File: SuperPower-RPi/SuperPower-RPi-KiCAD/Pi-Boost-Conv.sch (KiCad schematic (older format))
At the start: 0 parts

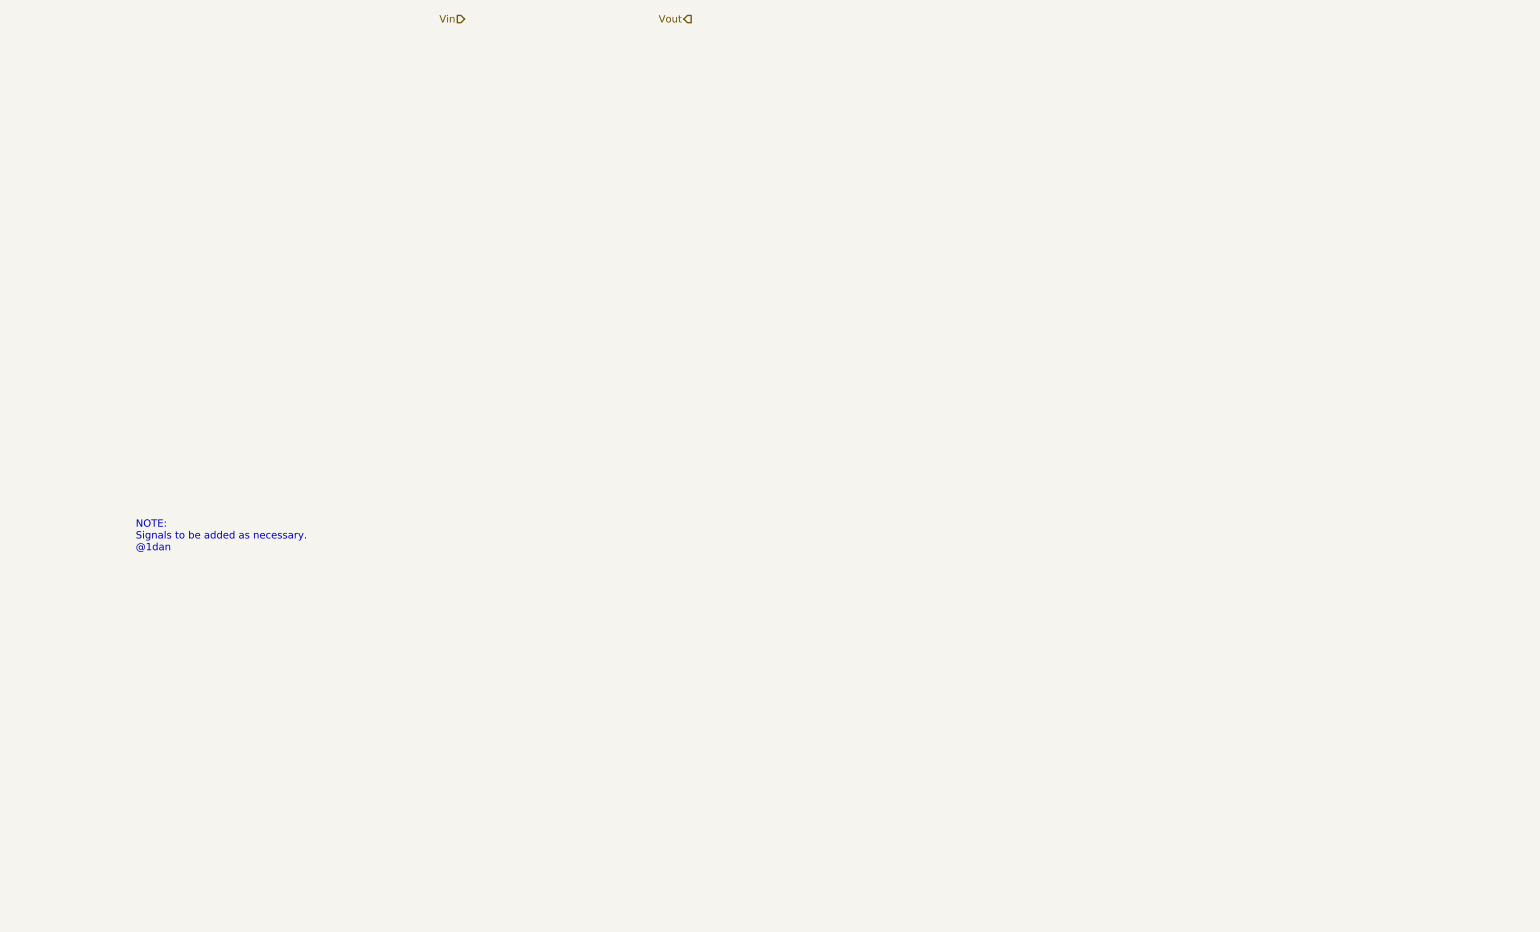
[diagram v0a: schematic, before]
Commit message: Basic component setup for the boost converter, added TPS61088 symbol to 'Manual_Lib' Library
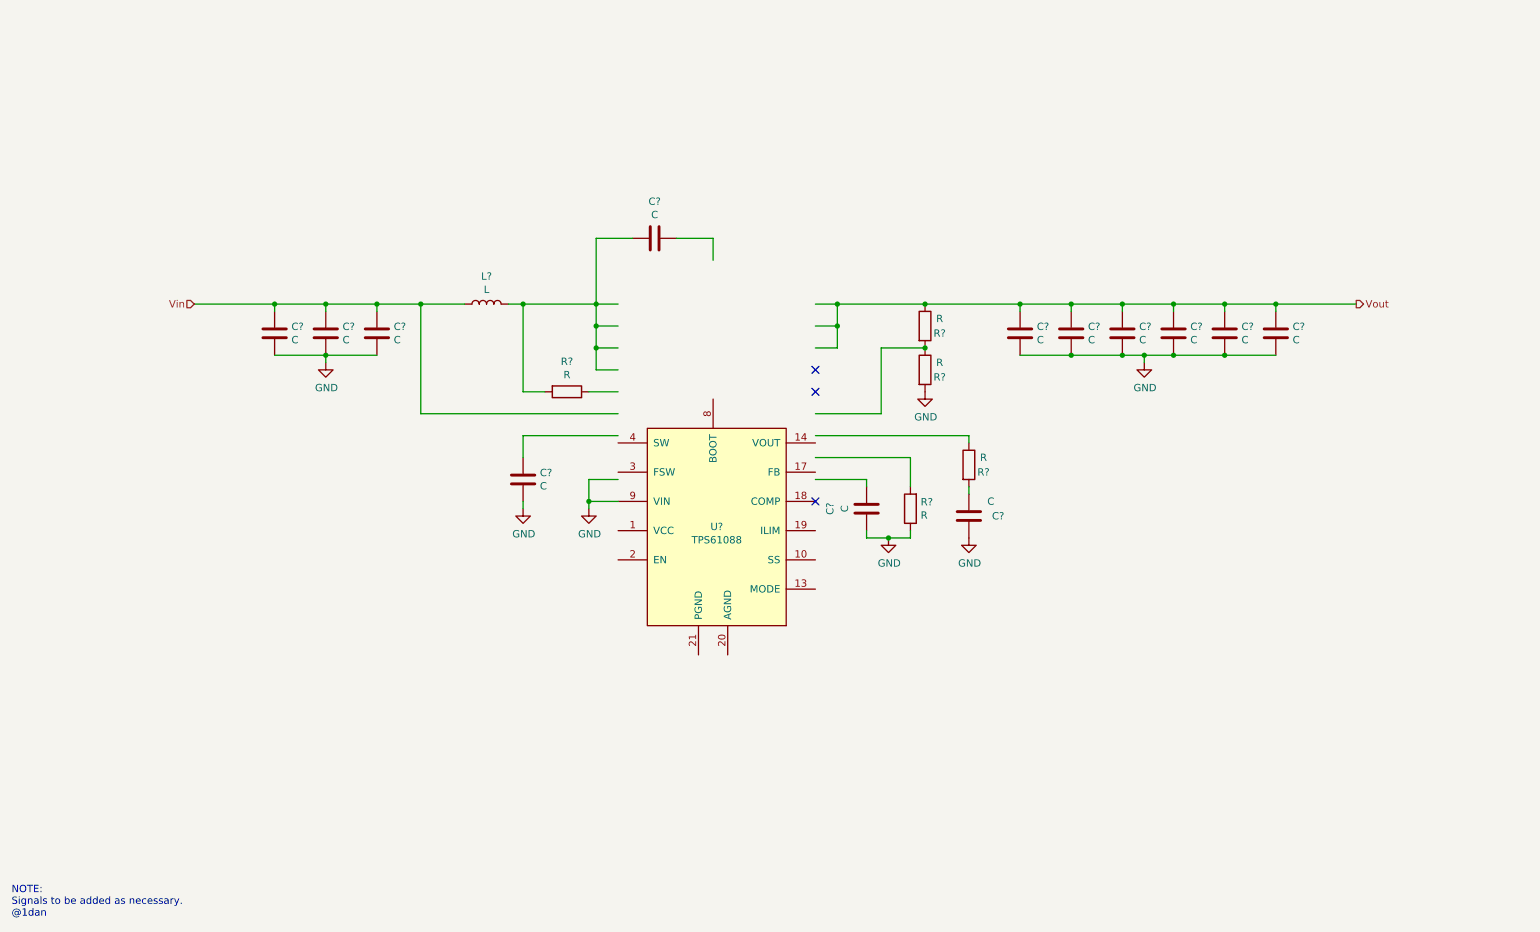
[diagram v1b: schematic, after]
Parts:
- added C? (x13): C, symbol Device:C
- added L?: L, symbol Device:L
- added R? (x5): R, symbol Device:R
- added U?: TPS61088, symbol Manual_Lib:TPS61088
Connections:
- net labels added: GND
- wire segments 0 -> 76
- no-connect marks 0 -> 3

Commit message: Basic component values added to boost ocnverter
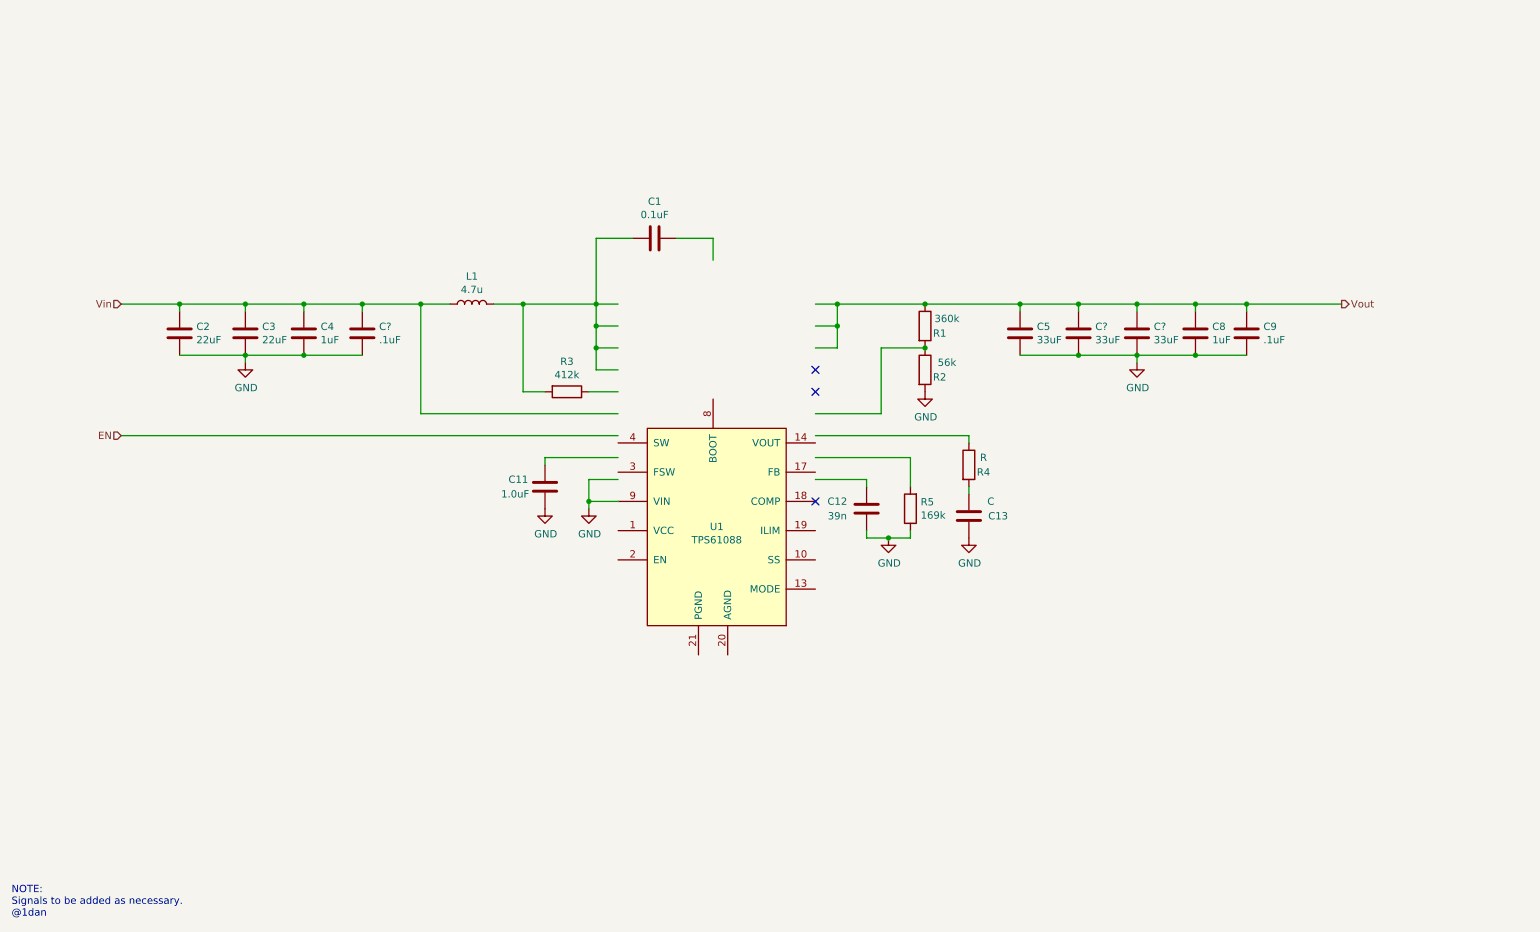
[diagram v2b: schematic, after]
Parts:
- removed C? (x3): C, symbol Device:C
- removed U?: TPS61088, symbol Manual_Lib:TPS61088
- added C? (x2): 33uF, symbol Device:C
- added C?: .1uF, symbol Device:C
- added U1: TPS61088, symbol Manual_Lib:TPS61088
- C1: renamed from C?; value C -> 0.1uF
- C11: renamed from C?; value C -> 1.0uF
- C12: renamed from C?; value C -> 39n
- C2, C3: renamed from C?; value C -> 22uF
- C4, C8: renamed from C?; value C -> 1uF
- C5: renamed from C?; value C -> 33uF
- C9: renamed from C?; value C -> .1uF
- L1: renamed from L?; value L -> 4.7u
- R1: renamed from R?; value R -> 360k
- R2: renamed from R?; value R -> 56k
- R3: renamed from R?; value R -> 412k
- R5: renamed from R?; value R -> 169k
- gave numbers to parts that had none: 2
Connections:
- net labels added: EN
- wire segments 76 -> 75
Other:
- moved on the sheet: C11, C2, C3, C4, C8, C9, L1

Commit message: Added charger circuitry, and updated boost converter.
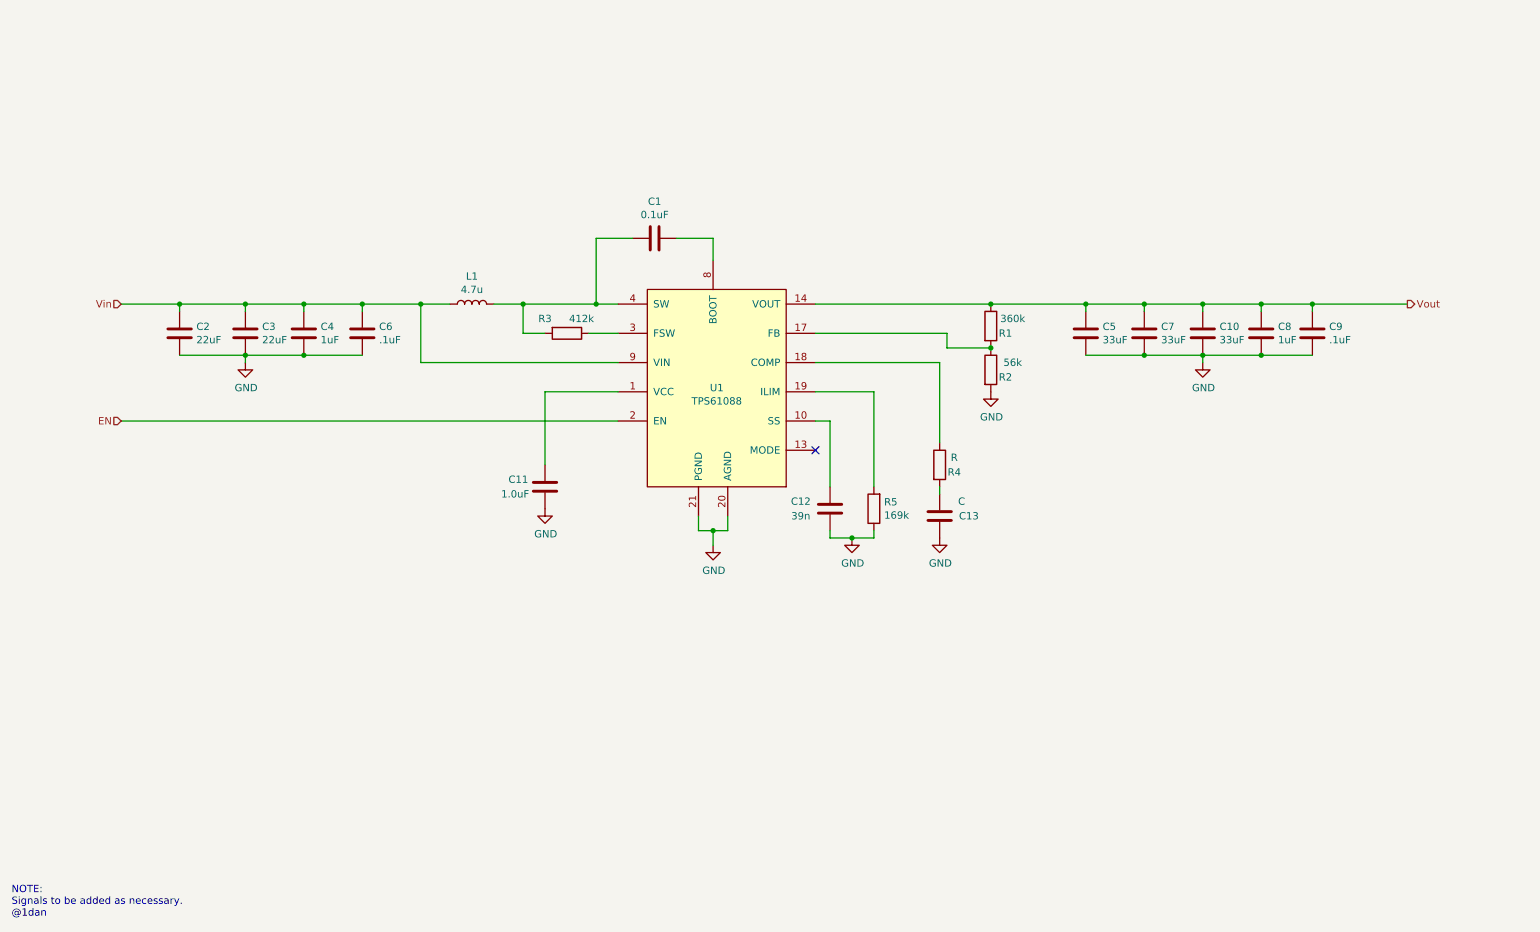
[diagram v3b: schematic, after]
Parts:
- gave numbers to parts that had none: 3
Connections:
- wire segments 75 -> 65
- no-connect marks 3 -> 1
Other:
- moved on the sheet: C10, C12, C13, C5, C7, C8, C9, R1, R2, R3, R4, R5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

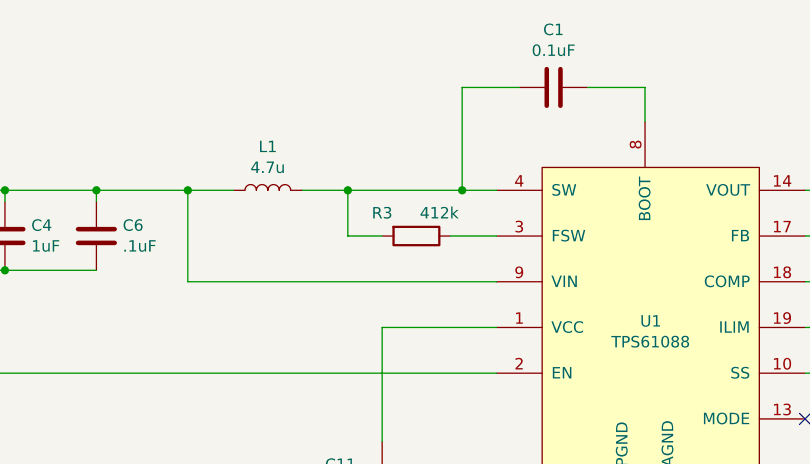
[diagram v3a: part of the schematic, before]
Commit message: Updated TPS61088 part to clear up ERC errors.
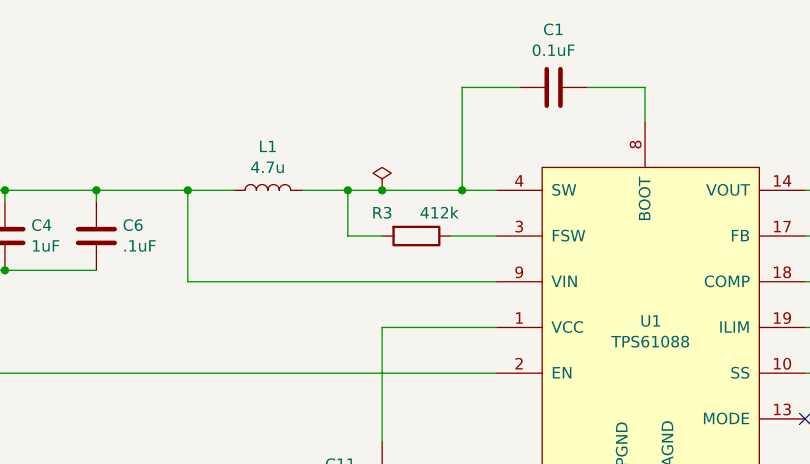
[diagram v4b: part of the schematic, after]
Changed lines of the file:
@@
 	4650 3400 4800 3400
 Wire Wire Line
-	4650 3400 4150 3400
+	4650 3400 4300 3400
 Connection ~ 4650 3400
 Wire Wire Line
@@
 Wire Wire Line
 	7000 3800 7000 4350
+$Comp
+L power:PWR_FLAG #FLG0105
+U 1 1 5F799D48
+P 4300 3400
+F 0 "#FLG0105" H 4300 3475 50  0001 C CNN
+F 1 "PWR_FLAG" H 4300 3573 50  0001 C CNN
+F 2 "" H 4300 3400 50  0001 C CNN
+F 3 "~" H 4300 3400 50  0001 C CNN
+	1    4300 3400
+	1    0    0    -1
+$EndComp
+Connection ~ 4300 3400
+Wire Wire Line
+	4300 3400 4150 3400
 $EndSCHEMATC

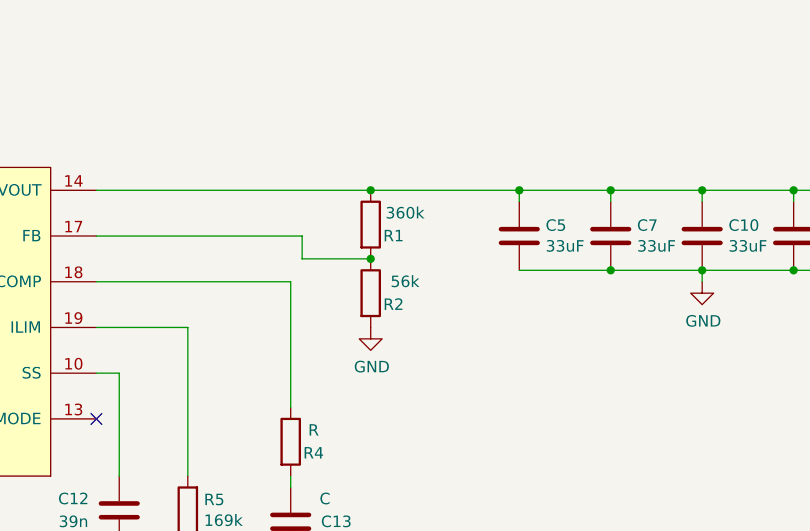
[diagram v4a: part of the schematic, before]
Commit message: Updated Boost Converter's feedback Resistor values
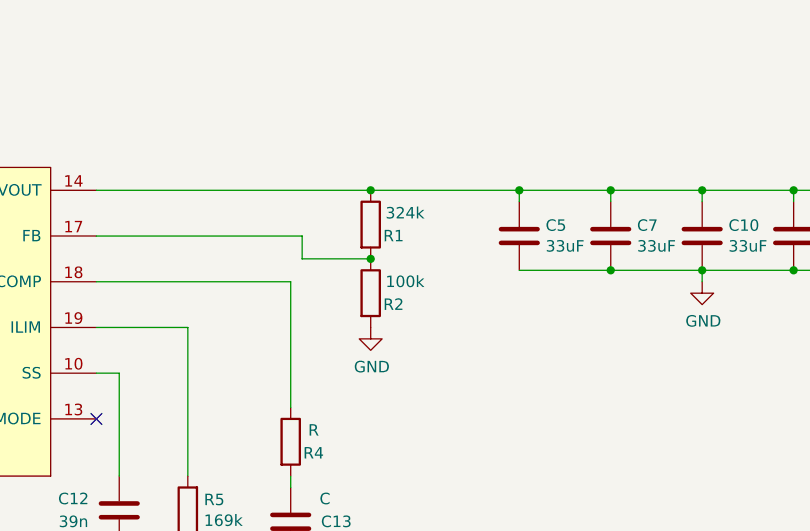
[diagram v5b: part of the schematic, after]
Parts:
- R1: value 360k -> 324k
- R2: value 56k -> 100k
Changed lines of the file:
@@
 P 7350 3850
 F 0 "R2" H 7450 3800 50  0000 C CNN
-F 1 "56k" H 7500 3900 50  0000 C CNN
+F 1 "100k" H 7500 3900 50  0000 C CNN
 F 2 "" V 7280 3850 50  0001 C CNN
 F 3 "~" H 7350 3850 50  0001 C CNN
@@
 P 7350 3550
 F 0 "R1" H 7450 3500 50  0000 C CNN
-F 1 "360k" H 7500 3600 50  0000 C CNN
+F 1 "324k" H 7500 3600 50  0000 C CNN
 F 2 "" V 7280 3550 50  0001 C CNN
 F 3 "~" H 7350 3550 50  0001 C CNN

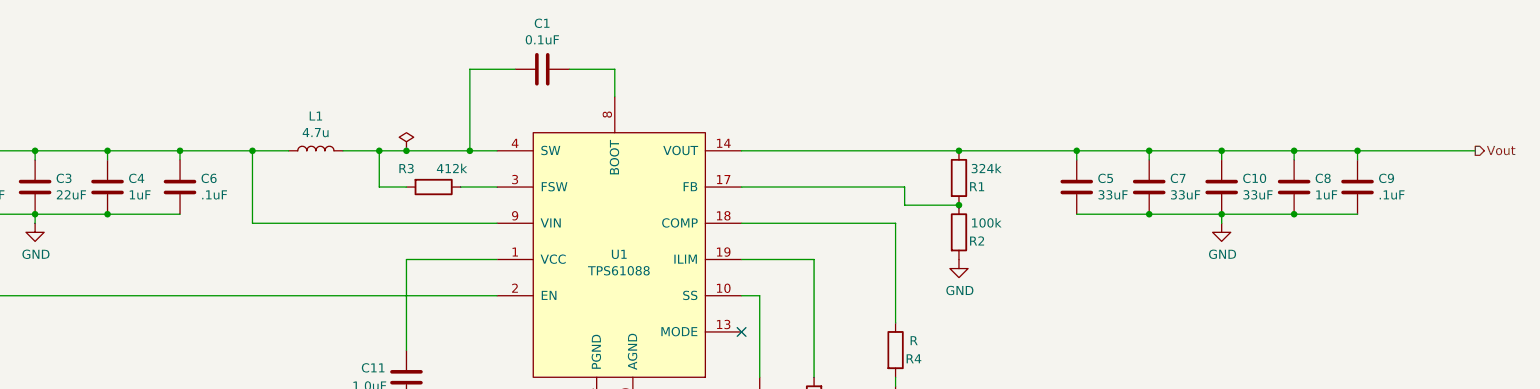
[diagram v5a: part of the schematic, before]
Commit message: Added overvoltag protection. Discussed on discord on 10/10/2020
(cherry picked from commit 123c8c775d478169a35a5854a68dc219ac457a44)
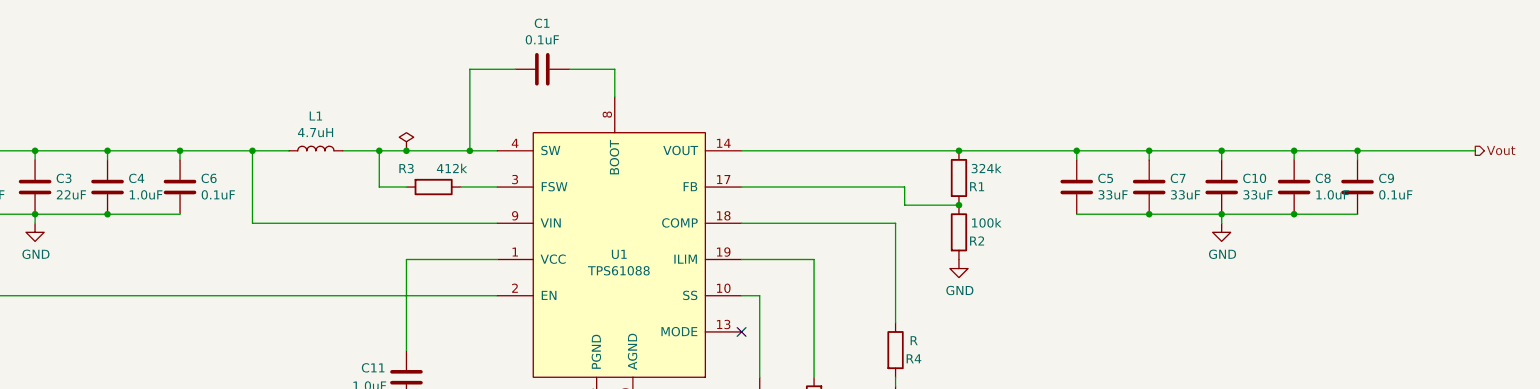
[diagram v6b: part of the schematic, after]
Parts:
- C1, C12: footprint (none) -> Capacitor_SMD:C_0603_1608Metric
- C4, C8: value 1uF -> 1.0uF
- C6, C9: value .1uF -> 0.1uF; footprint (none) -> Capacitor_SMD:C_0603_1608Metric
- L1: value 4.7u -> 4.7uH
- R1, R2, R3: footprint (none) -> Resistor_SMD:R_0603_1608Metric
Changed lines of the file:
@@
 P 3800 3400
 F 0 "L1" V 3990 3400 50  0000 C CNN
-F 1 "4.7u" V 3899 3400 50  0000 C CNN
+F 1 "4.7uH" V 3899 3400 50  0000 C CNN
 F 2 "" H 3800 3400 50  0001 C CNN
 F 3 "~" H 3800 3400 50  0001 C CNN
@@
 F 0 "R3" V 4350 3450 50  0000 C CNN
 F 1 "412k" V 4350 3700 50  0000 C CNN
-F 2 "" V 4380 3600 50  0001 C CNN
+F 2 "Resistor_SMD:R_0603_1608Metric" V 4380 3600 50  0001 C CNN
 F 3 "~" H 4450 3600 50  0001 C CNN
 	1    4450 3600
@@
 P 2650 3600
 F 0 "C4" H 2765 3646 50  0000 L CNN
-F 1 "1uF" H 2765 3555 50  0000 L CNN
+F 1 "1.0uF" H 2765 3555 50  0000 L CNN
 F 2 "" H 2688 3450 50  0001 C CNN
 F 3 "~" H 2650 3600 50  0001 C CNN
@@
 P 9200 3600
 F 0 "C8" H 9315 3646 50  0000 L CNN
-F 1 "1uF" H 9315 3555 50  0000 L CNN
+F 1 "1.0uF" H 9315 3555 50  0000 L CNN
 F 2 "" H 9238 3450 50  0001 C CNN
 F 3 "~" H 9200 3600 50  0001 C CNN
@@
 P 9550 3600
 F 0 "C9" H 9665 3646 50  0000 L CNN
-F 1 ".1uF" H 9665 3555 50  0000 L CNN
-F 2 "" H 9588 3450 50  0001 C CNN
+F 1 "0.1uF" H 9665 3555 50  0000 L CNN
+F 2 "Capacitor_SMD:C_0603_1608Metric" H 9588 3450 50  0001 C CNN
 F 3 "~" H 9550 3600 50  0001 C CNN
 	1    9550 3600
@@
 F 0 "C1" V 4798 2950 50  0000 C CNN
 F 1 "0.1uF" V 4889 2950 50  0000 C CNN
-F 2 "" H 5088 2800 50  0001 C CNN
+F 2 "Capacitor_SMD:C_0603_1608Metric" H 5088 2800 50  0001 C CNN
 F 3 "~" H 5050 2950 50  0001 C CNN
 	1    5050 2950
@@
 F 0 "R2" H 7450 3800 50  0000 C CNN
 F 1 "100k" H 7500 3900 50  0000 C CNN
-F 2 "" V 7280 3850 50  0001 C CNN
+F 2 "Resistor_SMD:R_0603_1608Metric" V 7280 3850 50  0001 C CNN
 F 3 "~" H 7350 3850 50  0001 C CNN
 	1    7350 3850
@@
 F 0 "R1" H 7450 3500 50  0000 C CNN
 F 1 "324k" H 7500 3600 50  0000 C CNN
-F 2 "" V 7280 3550 50  0001 C CNN
+F 2 "Resistor_SMD:R_0603_1608Metric" V 7280 3550 50  0001 C CNN
 F 3 "~" H 7350 3550 50  0001 C CNN
 	1    7350 3550
@@
 P 3050 3600
 F 0 "C6" H 3165 3646 50  0000 L CNN
-F 1 ".1uF" H 3165 3555 50  0000 L CNN
-F 2 "" H 3088 3450 50  0001 C CNN
+F 1 "0.1uF" H 3165 3555 50  0000 L CNN
+F 2 "Capacitor_SMD:C_0603_1608Metric" H 3088 3450 50  0001 C CNN
 F 3 "~" H 3050 3600 50  0001 C CNN
 	1    3050 3600
@@
 F 0 "C12" H 6050 4750 50  0000 C CNN
 F 1 "39n" H 6050 4850 50  0000 C CNN
-F 2 "" H 6288 4650 50  0001 C CNN
+F 2 "Capacitor_SMD:C_0603_1608Metric" H 6288 4650 50  0001 C CNN
 F 3 "~" H 6250 4800 50  0001 C CNN
 	1    6250 4800
